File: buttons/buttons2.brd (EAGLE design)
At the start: 70 x 44 mm, 14 parts, among them U1 attiny2313

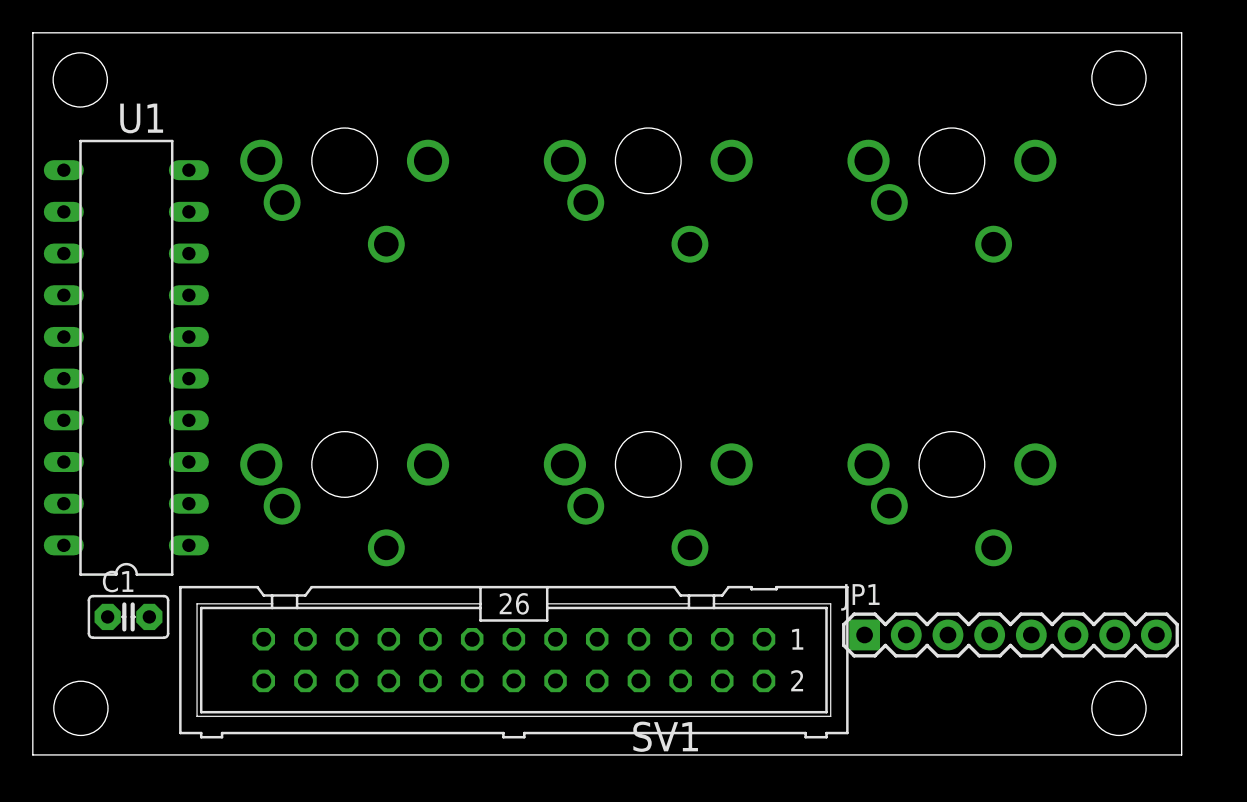
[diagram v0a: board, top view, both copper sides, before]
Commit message: finished routing updated buttons2 PCB
This has (I think) adequate clearance for an 18mm x 18mm
keycap: the centers of the switches are 18.5mm apart, hopefully
this is enough room.
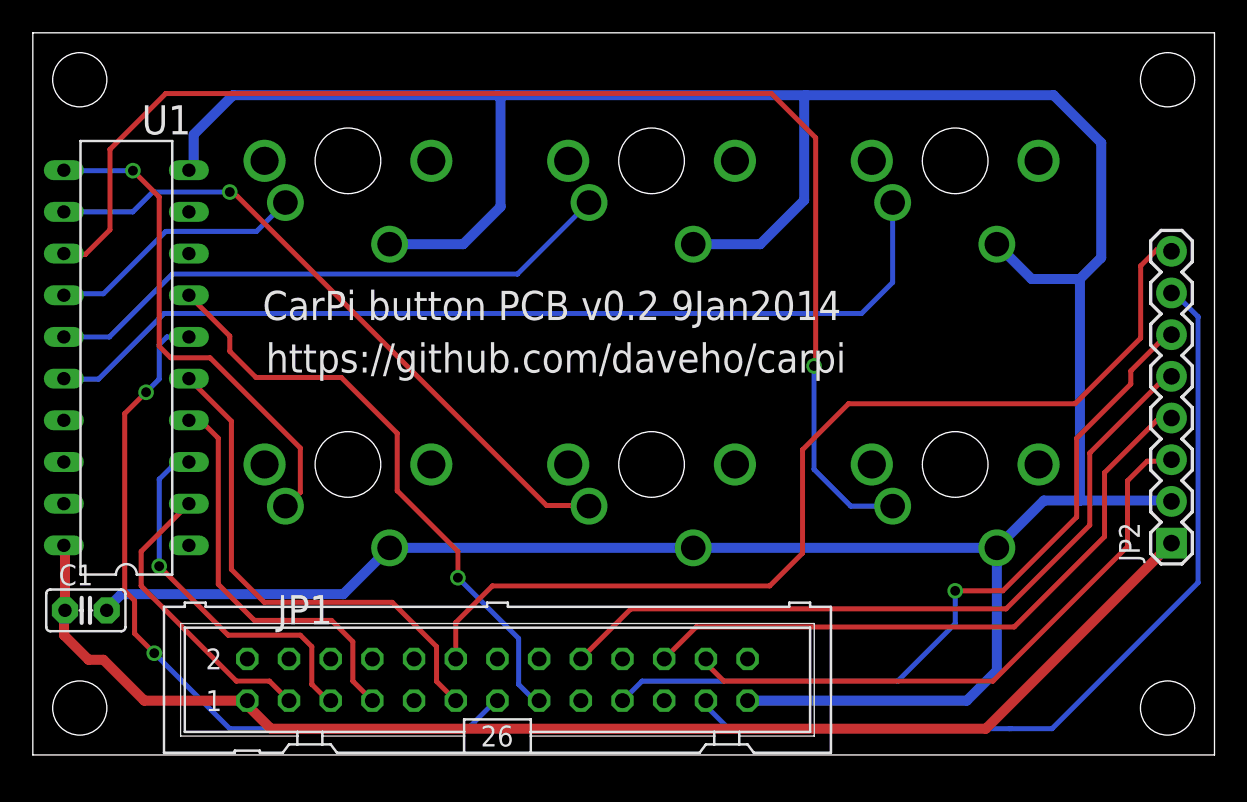
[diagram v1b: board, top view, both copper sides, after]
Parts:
- removed SV1: RPi_GPIO, con-harting-ml:ML26
- added JP2: LCD_CONN, SparkFun-Connectors:1X08
- JP1: value LCD_CONN -> RPi_GPIO; device SparkFun-Connectors:1X08 -> con-harting-ml:ML26
- moved JP1 22.5 mm to (28.3, 4.58)
- moved STANDOFF3 2.96 mm to (69.1, 41.1)
- moved STANDOFF1 2.96 mm to (69.1, 2.86)
- moved C1 2.63 mm to (3.23, 8.81)
- moved S2 0.20 mm to (37.7, 17.7)
- moved S3 0.20 mm to (56.2, 17.7)
- moved S5 0.20 mm to (37.7, 36.2)
- moved S6 0.20 mm to (56.2, 36.2)
- moved S1 0.20 mm to (19.2, 17.7)
- moved S4 0.20 mm to (19.2, 36.2)
- moved STANDOFF2 0.07 mm to (2.86, 2.86)
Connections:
- net BUTTON1: now also JP1.3; no longer SV1.3
- net BUTTON2: now also JP1.5; no longer SV1.5
- net BUTTON3: now also JP1.7; no longer SV1.7
- net BUTTON4: now also JP1.11; no longer SV1.11
- net BUTTON5: now also JP1.13; no longer SV1.13
- net BUTTON6: now also JP1.15; no longer SV1.15
- net CS: now also JP1.24, JP2.3; no longer JP1.3, SV1.24
- net DC: now also JP1.18, JP2.5; no longer JP1.5, SV1.18
- net GND: now also JP1.25, JP2.2; no longer JP1.2, SV1.25
- net LED: now also JP1.12, JP2.8; no longer JP1.8, SV1.12
- net MOSI: now also JP1.19, JP2.6; no longer JP1.6, SV1.19
- net RESET: now also JP1.22, JP2.4; no longer JP1.4, SV1.22
- net SCK: now also JP1.23, JP2.7; no longer JP1.7, SV1.23
- net VCC: now also JP2.1; no longer SV1.1
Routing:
- net GND: track 0.00 -> 208.3 mm
- net VCC: track 0.00 -> 80.2 mm
- net N$4: track 0.00 -> 79.7 mm, vias 0 -> 1
- net LED: track 0.00 -> 61.6 mm
- net N$1: track 0.00 -> 57.8 mm
- net SCK: track 0.00 -> 53.0 mm
- net MOSI: track 0.00 -> 47.1 mm, vias 0 -> 1
- net BUTTON5: track 0.00 -> 45.9 mm, vias 0 -> 2
- net DC: track 0.00 -> 45.7 mm
- net N$5: track 0.00 -> 40.4 mm, vias 0 -> 1
- net RESET: track 0.00 -> 39.3 mm
- net CS: track 0.00 -> 37.0 mm
- net BUTTON6: track 0.00 -> 36.7 mm, vias 0 -> 1
- net N$2: track 0.00 -> 35.4 mm
- net BUTTON4: track 0.00 -> 30.9 mm
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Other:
- board size 70 x 44 mm -> 72 x 44 mm
- board text added: "CarPi button PCB v0.2 9Jan2014"
- board text added: "https://github.com/daveho/carpi"

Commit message: some minor routing tweaks
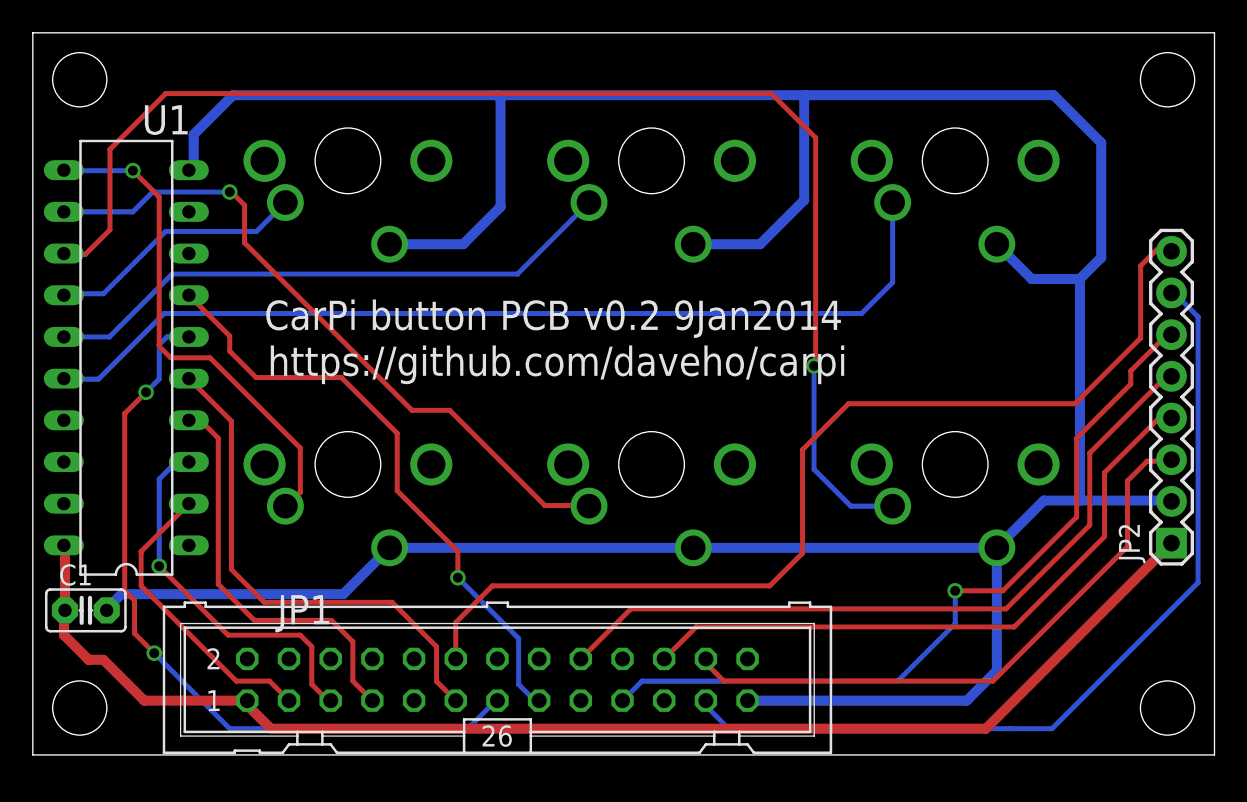
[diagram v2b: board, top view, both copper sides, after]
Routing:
- net N$5: track 40.4 -> 42.0 mm
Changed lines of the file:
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@@
 <wire x1="72" y1="44" x2="0" y2="44" width="0" layer="20"/>
 <wire x1="0" y1="44" x2="0" y2="0" width="0" layer="20"/>
-<text x="14" y="26.5" size="1.778" layer="21" font="vector">CarPi button PCB v0.2 9Jan2014</text>
-<text x="14.2" y="23.3" size="1.778" layer="21" font="vector">https://github.com/daveho/carpi</text>
+<text x="14.1" y="25.9" size="1.778" layer="21" font="vector">CarPi button PCB v0.2 9Jan2014</text>
+<text x="14.3" y="23.1" size="1.778" layer="21" font="vector">https://github.com/daveho/carpi</text>
 </plain>
 <attributes>
@@
 <wire x1="8.1" y1="40.3" x2="4.7" y2="36.9" width="0.3048" layer="1"/>
 <wire x1="4.7" y1="36.9" x2="4.7" y2="32" width="0.3048" layer="1"/>
-<wire x1="47.7" y1="23.8" x2="47.6" y2="23.7" width="0" layer="19" extent="1-1"/>
 <wire x1="4.7" y1="32" x2="3.2" y2="30.5" width="0.3048" layer="1"/>
 <wire x1="3.2" y1="30.5" x2="1.94" y2="30.5" width="0.3048" layer="1"/>
 <wire x1="1.94" y1="30.5" x2="1.89" y2="30.55" width="0.3048" layer="1"/>
+<wire x1="47.7" y1="23.8" x2="47.6" y2="23.7" width="0" layer="19" extent="1-1"/>
 </signal>
 <signal name="N$5">
@@
 <via x="12" y="34.3" extent="1-16" drill="0.6"/>
 <wire x1="12" y1="34.3" x2="12.2" y2="34.3" width="0.3048" layer="1"/>
-<wire x1="12.2" y1="34.3" x2="31.3" y2="15.2" width="0.3048" layer="1"/>
-<wire x1="31.3" y1="15.2" x2="33.85" y2="15.2" width="0.3048" layer="1"/>
+<wire x1="31.2" y1="15.2" x2="33.85" y2="15.2" width="0.3048" layer="1"/>
 <wire x1="33.85" y1="15.2" x2="33.89" y2="15.16" width="0.3048" layer="1"/>
+<wire x1="12" y1="34.3" x2="12.1" y2="34.3" width="0.3048" layer="1"/>
+<wire x1="12.1" y1="34.3" x2="12.9" y2="33.5" width="0.3048" layer="1"/>
+<wire x1="12.9" y1="33.5" x2="12.9" y2="31.2" width="0.3048" layer="1"/>
+<wire x1="12.9" y1="31.2" x2="23.1" y2="21" width="0.3048" layer="1"/>
+<wire x1="23.1" y1="21" x2="25.4" y2="21" width="0.3048" layer="1"/>
+<wire x1="31.2" y1="15.2" x2="25.4" y2="21" width="0.3048" layer="1"/>
 </signal>
 <signal name="N$6">
